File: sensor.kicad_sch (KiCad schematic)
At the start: 8 parts, among them U2 ICM-42688-P

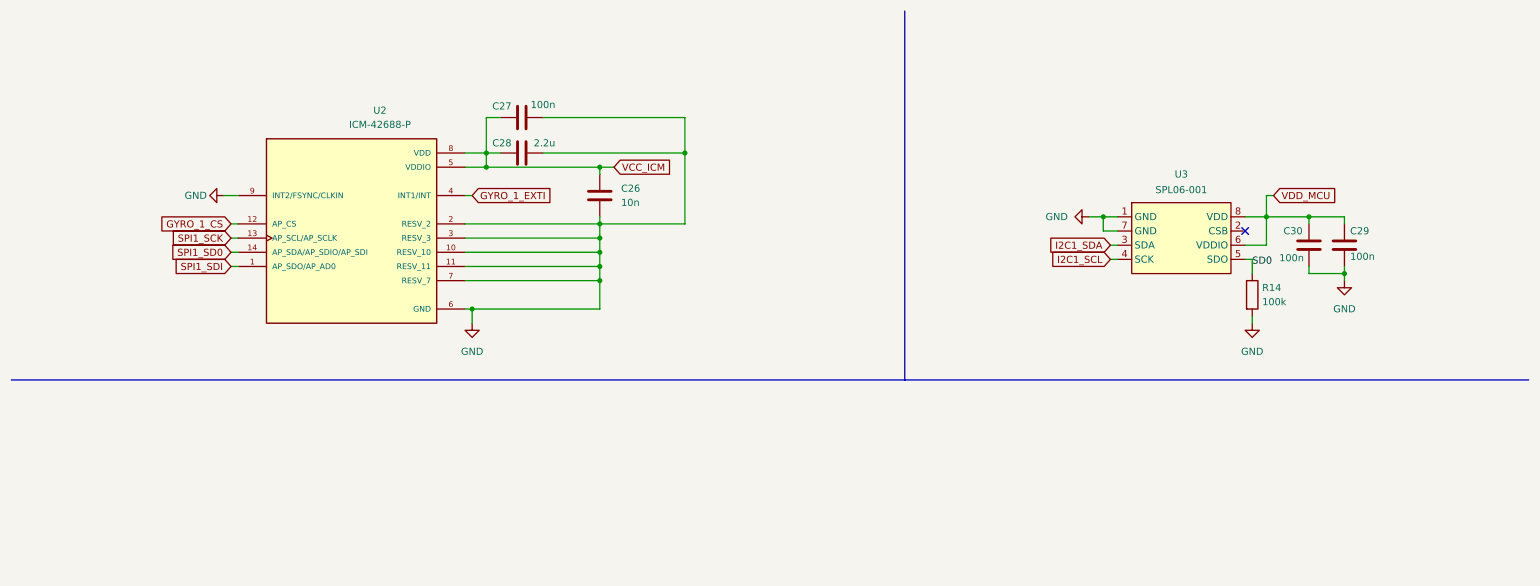
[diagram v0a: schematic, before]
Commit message: changed barometer to BMP580 and completed BOM
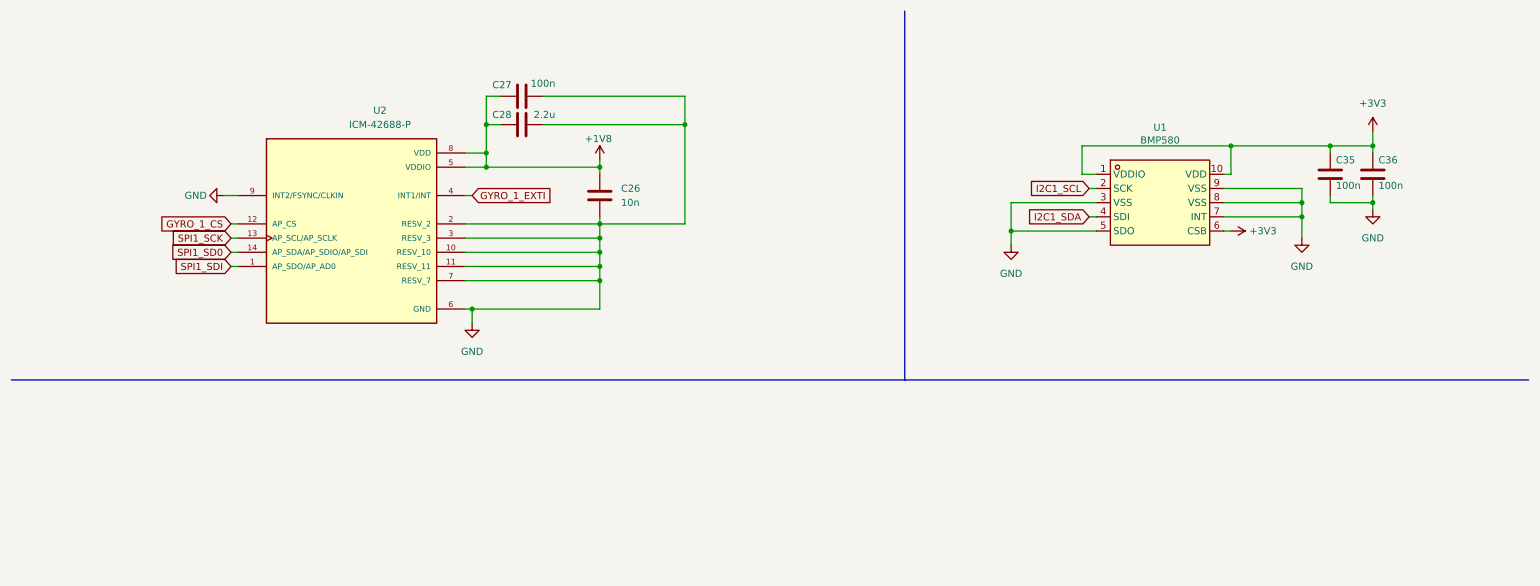
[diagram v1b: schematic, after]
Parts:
- removed C29, C30: 100n, Capacitor_SMD:C_0603_1608Metric, symbol Device:C
- removed R14: 100k, Resistor_SMD:R_0603_1608Metric, symbol Device:R
- removed U3: ~, ProLib_pcs_2026-02-12:SENSOR-SMD_SPL06-001, symbol fcg4:SPL06-001
- added C35, C36: 100n, Capacitor_SMD:C_0603_1608Metric, symbol Device:C
- added U1: BMP580, fcg4_fp:LGA-10_L2.0-W2.0-P0.50-TL_BMP580, symbol fcg4:BMP580
- C26: LCSC Part Name C91601 -> C1589; Manufacturer_Name muRata -> Samsung Electro-Mechanics; Manufacturer_Part_Number GCM155R71H103KA55D -> CL10B103KB8NNNC
- C27: LCSC Part Name C77020 -> C1591; Manufacturer_Name muRata -> Samsung Electro-Mechanics; Manufacturer_Part_Number GRM155R71H104KE14D -> CL10B104KB8NNNC
- C28: LCSC Part Name C385032 -> C913904; Manufacturer_Name muRata -> Samsung Electro-Mechanics; Manufacturer_Part_Number GRM155R61E225KE11D -> CL10A225KB8NNNC
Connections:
- net GND: now also C35.1, C36.1, U1.3 (VSS), U1.5 (SDO), U1.7 (INT), U1.8 (VSS), U1.9 (VSS)
- net I2C1_SCL: now also U1.2 (SCK)
- net I2C1_SDA: now also U1.4 (SDI)
- net VCC_ICM renamed +1V8
- new net +3V3: C35.2, C36.2, U1.1 (VDDIO), U1.10 (VDD), U1.6 (CSB)
- no-connect marks 1 -> 0
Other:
- moved on the sheet: C27, C28

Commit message: switch IMU to BMI270
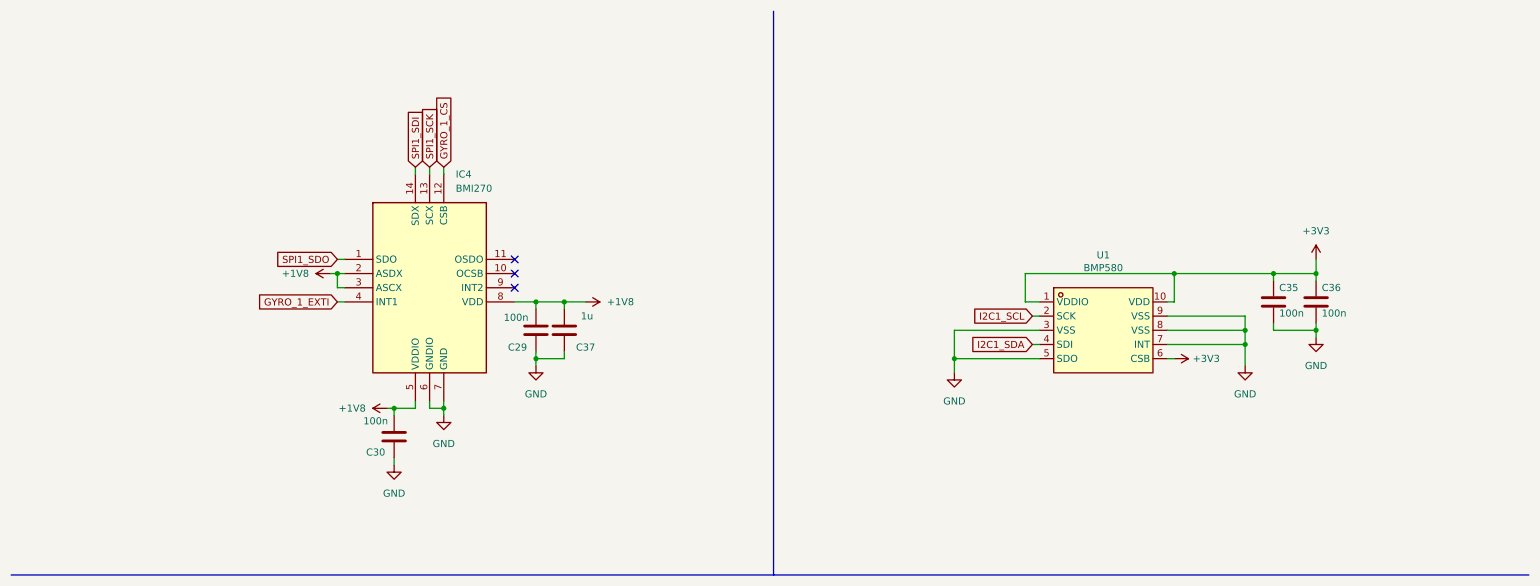
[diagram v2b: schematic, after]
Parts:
- removed C26: 10n, Capacitor_SMD:C_0603_1608Metric, symbol Device:C
- removed C27: 100n, Capacitor_SMD:C_0603_1608Metric, symbol Device:C
- removed C28: 2.2u, Capacitor_SMD:C_0603_1608Metric, symbol Device:C
- removed U2: ICM-42688-P, fcg4_fp:PQFN50P300X250X97-14N, symbol fcg4:ICM-42688-P
- added C29, C30: 100n, Capacitor_SMD:C_0603_1608Metric, symbol Device:C
- added C37: 1u, Capacitor_SMD:C_0603_1608Metric, symbol Device:C
- added IC4: BMI270, fcg4_fp:BMI270, symbol fcg4:BMI270
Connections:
- net +1V8: now also C29.2, C30.2, C37.2, IC4.2 (ASDX), IC4.3 (ASCX), IC4.5 (VDDIO), IC4.8 (VDD)
- net GND: now also C29.1, C30.1, C37.1, IC4.6 (GNDIO), IC4.7 (GND)
- net GYRO_1_CS: now also IC4.12 (CSB)
- net GYRO_1_EXTI: now also IC4.4 (INT1)
- net SPI1_SCK: now also IC4.13 (SCX)
- net SPI1_SDI: now also IC4.14 (SDX)
- new net SPI1_SDO: IC4.1 (SDO)
- no-connect marks 0 -> 3
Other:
- moved on the sheet: C35, C36, U1

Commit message: add microsd card connector
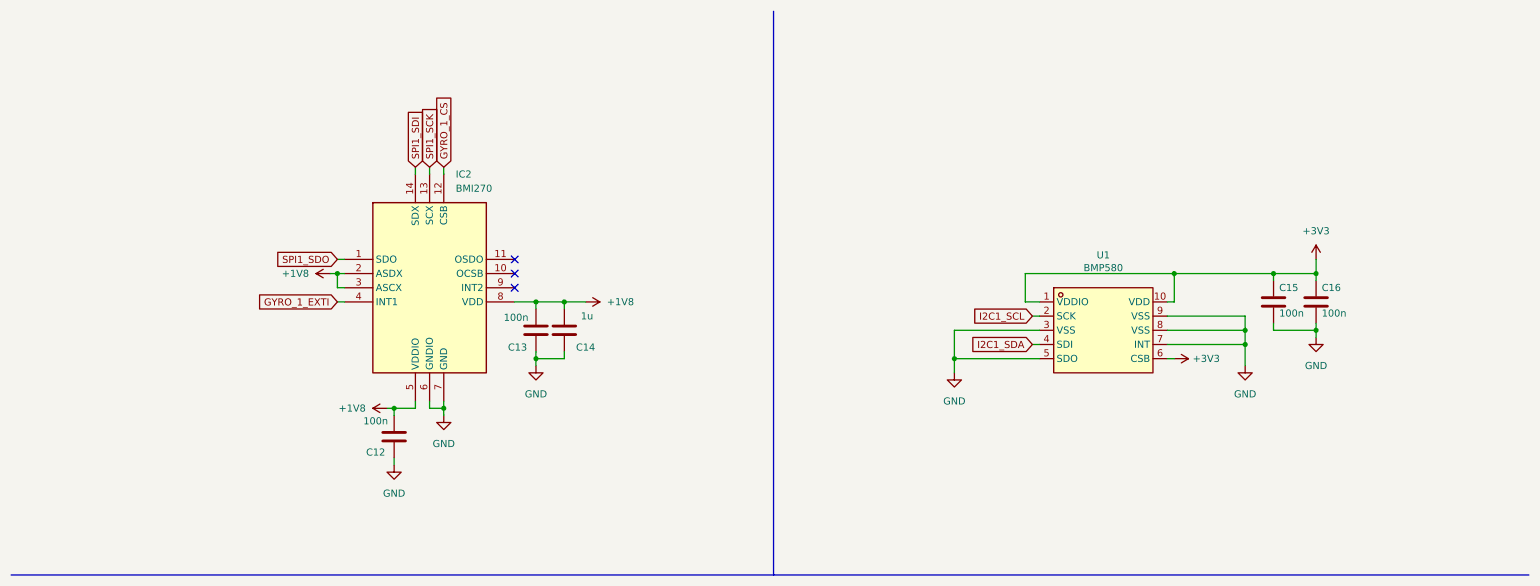
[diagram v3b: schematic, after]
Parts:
- U1: Manufacturer Bosch -> (none)
- renumbered C30 to C12, C29 to C13, C37 to C14, C35 to C15, C36 to C16, IC4 to IC2
